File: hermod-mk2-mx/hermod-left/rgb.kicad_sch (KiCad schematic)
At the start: 76 parts

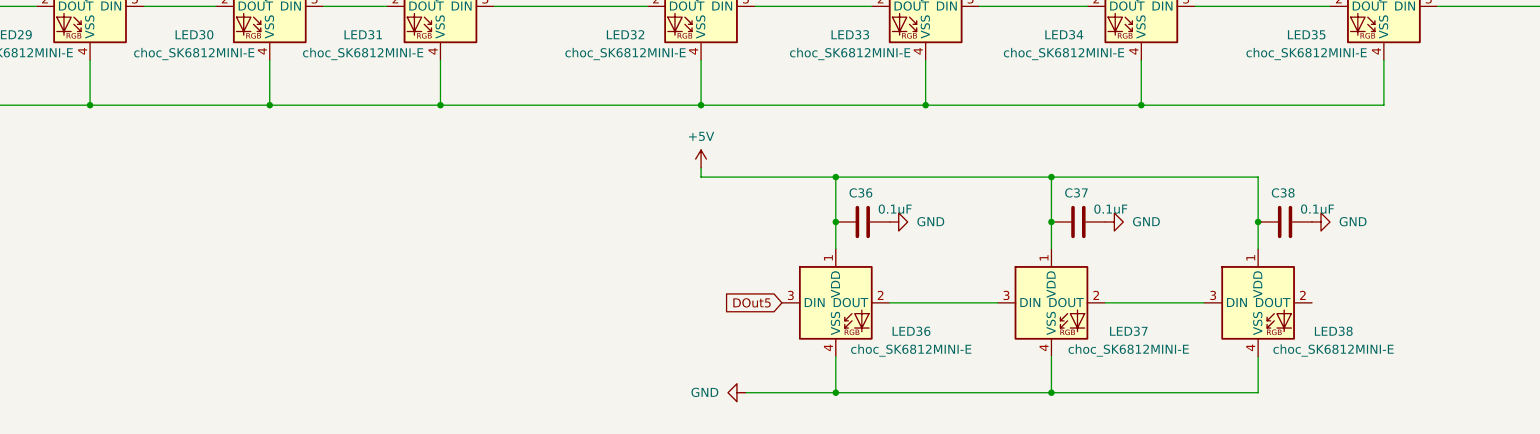
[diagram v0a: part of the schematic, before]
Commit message: Added switches to hermod 3 and updated mist thumb spacing
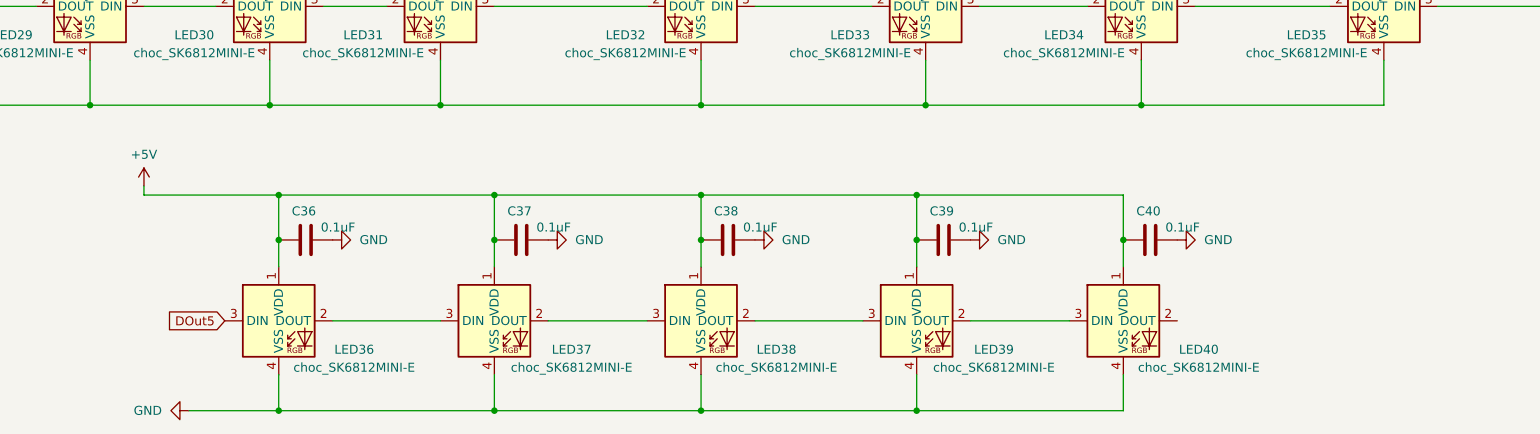
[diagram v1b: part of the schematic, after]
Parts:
- added C39, C40: 0.1uF, Capacitor_SMD:C_0402_1005Metric, symbol Device:C
- added LED39, LED40: choc_SK6812MINI-E, PCM_marbastlib-choc:LED_choc_6028R, symbol PCM_marbastlib-choc:choc_SK6812MINI-E
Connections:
- net +5V: now also C39.1, C40.1, LED39.1 (VDD), LED40.1 (VDD)
- net GND: now also C39.2, C40.2, LED39.4 (VSS), LED40.4 (VSS)
- net at LED38.2 (DOUT): now also LED39.3 (DIN)
- new net: LED39.2 (DOUT), LED40.3 (DIN)
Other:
- moved on the sheet: C36, C37, C38, LED36, LED37, LED38
